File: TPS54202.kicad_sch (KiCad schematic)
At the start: 13 parts, among them U3 TPS54202DDC

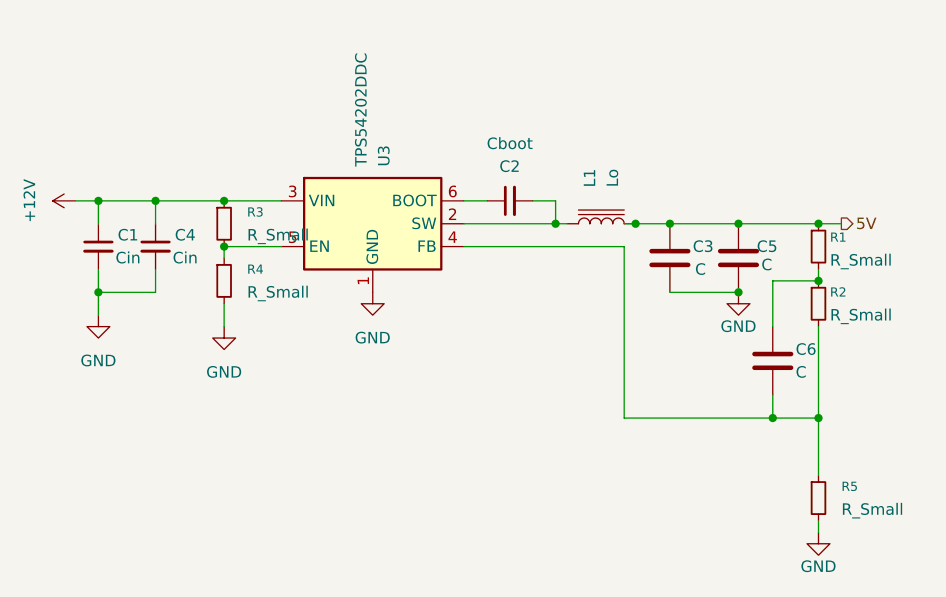
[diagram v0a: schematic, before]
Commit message: incomplete calcs for TPS
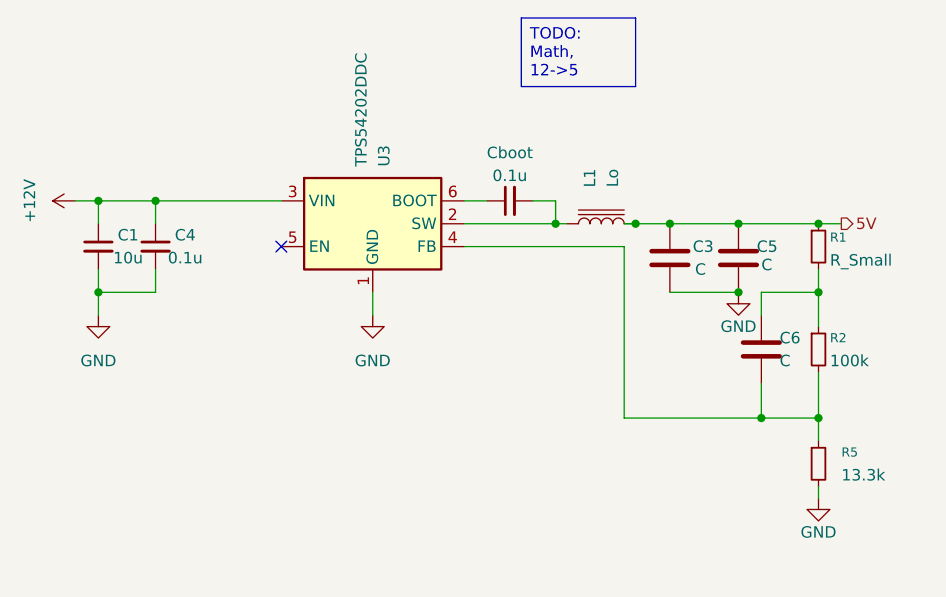
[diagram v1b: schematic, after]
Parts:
- removed R3, R4: R_Small, symbol Device:R_Small
- C1: value Cin -> 10u
- C4: value Cin -> 0.1u
- R2: value R_Small -> 100k
- R5: value R_Small -> 13.3k
- renumbered C2 to 0.1u
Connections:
- no-connect marks 0 -> 1
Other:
- moved on the sheet: C6, R2, R5

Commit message: finished math
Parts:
- removed R1: R_Small, symbol Device:R_Small
- C3, C5: value C -> 22u
- C6: value C -> 75p
- L1: value Lo -> 20u
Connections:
- net 5V: now also C6.1, R2.1
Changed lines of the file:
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@@
 	(generator_version "9.0")
 	(paper "A4")
-	(text_box "TODO: Math, 12->5\n"
+	(text_box "12->5 Iout = 1.5A"
 		(exclude_from_sim no)
 		(at 129.54 45.72 0)
-		(size 12.7 7.62)
+		(size 12.7 8.89)
 		(margins 0.9525 0.9525 0.9525 0.9525)
 		(stroke
@@
 	)
 	(junction
+		(at 162.56 68.58)
+		(diameter 0)
+		(color 0 0 0 0)
+	)
+	(junction
 		(at 82.55 66.04)
 		(diameter 0)
@@
 	)
 	(junction
-		(at 162.56 68.58)
-		(diameter 0)
-		(color 0 0 0 0)
-	)
-	(junction
 		(at 82.55 76.2)
 		(diameter 0)
@@
 	(wire
 		(pts
+			(xy 153.67 68.58) (xy 162.56 68.58)
+		)
+		(stroke
+			(width 0)
+			(type default)
+		)
+	)
+	(wire
+		(pts
+			(xy 162.56 92.71) (xy 162.56 90.17)
+		)
+		(stroke
+			(width 0)
+			(type default)
+		)
+	)
+	(wire
+		(pts
+			(xy 82.55 76.2) (xy 88.9 76.2)
+		)
+		(stroke
+			(width 0)
+			(type default)
+		)
+	)
+	(wire
+		(pts
 			(xy 162.56 68.58) (xy 165.1 68.58)
 		)
@@
 	(wire
 		(pts
-			(xy 162.56 92.71) (xy 162.56 90.17)
-		)
-		(stroke
-			(width 0)
-			(type default)
-		)
-	)
-	(wire
-		(pts
-			(xy 82.55 76.2) (xy 88.9 76.2)
-		)
-		(stroke
-			(width 0)
-			(type default)
-		)
-	)
-	(wire
-		(pts
 			(xy 142.24 68.58) (xy 146.05 68.58)
 		)
@@
 	(wire
 		(pts
-			(xy 153.67 68.58) (xy 162.56 68.58)
-		)
-		(stroke
-			(width 0)
-			(type default)
-		)
-	)
-	(wire
-		(pts
 			(xy 140.97 68.58) (xy 142.24 68.58)
 		)
@@
 	(wire
 		(pts
-			(xy 162.56 73.66) (xy 162.56 76.2)
+			(xy 162.56 68.58) (xy 162.56 76.2)
 		)
 		(stroke
@@
 			)
 		)
-		(property "Value" "C"
+		(property "Value" "22u"
 			(at 156.21 73.152 0)
 			(effects
@@
 			)
 		)
-		(property "Value" "Lo"
+		(property "Value" "20u"
 			(at 139.7 63.5 0)
 			(effects
@@
 	)
 	(symbol
-		(lib_id "Device:R_Small")
-		(at 162.56 71.12 0)
-		(unit 1)
-		(exclude_from_sim no)
-		(in_bom yes)
-		(on_board yes)
-		(dnp no)
-		(property "Reference" "R1"
-			(at 163.83 70.104 0)
-			(effects
-				(font
-					(size 1.016 1.016)
-				)
-				(justify left)
-			)
-		)
-		(property "Value" "R_Small"
-			(at 163.83 72.644 0)
-			(effects
-				(font
-					(size 1.27 1.27)
-				)
-				(justify left)
-			)
-		)
-		(property "Footprint" ""
-			(at 162.56 71.12 0)
-			(effects
-				(font
-					(size 1.27 1.27)
-				)
-				(hide yes)
-			)
-		)
-		(property "Datasheet" "~"
-			(at 162.56 71.12 0)
-			(effects
-				(font
-					(size 1.27 1.27)
-				)
-				(hide yes)
-			)
-		)
-		(property "Description" "Resistor, small symbol"
-			(at 162.56 71.12 0)
-			(effects
-				(font
-					(size 1.27 1.27)
-				)
-				(hide yes)
-			)
-		)
-		(pin "2"
-		)
-		(pin "1"
-		)
-		(instances
-			(project "LightsAndSuch"
-				(path "/f2987657-b7e0-480f-b307-23af9e47acd8/94c2b8e7-7d05-4ea8-a2a7-7484a2eccb30"
-					(reference "R1")
-					(unit 1)
-				)
-			)
-		)
-	)
-	(symbol
 		(lib_id "Device:C")
 		(at 156.21 82.55 0)
@@
 			)
 		)
-		(property "Value" "C"
+		(property "Value" "75p"
 			(at 158.242 83.82 0)
 			(effects
@@
 		(dnp no)
 		(property "Reference" "C3"
-			(at 148.59 71.12 0)
+			(at 147.828 71.12 0)
 			(effects
 				(font
@@
 			)
 		)
-		(property "Value" "C"
-			(at 148.844 73.6599 0)
-			(effects
-				(font
+		(property "Value" "22u"
+			(at 148.082 73.6599 0)
+			(effects
+				(font

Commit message: added secondary circuit
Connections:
- net 5V renamed +5V
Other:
- moved on the sheet: C1, C4
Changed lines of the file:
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@@
-	)
-	(junction
-		(at 82.55 66.04)
-		(diameter 0)
-		(color 0 0 0 0)
 	)
 	(junction
@@
 	)
 	(junction
+		(at 95.25 66.04)
+		(diameter 0)
+		(color 0 0 0 0)
+	)
+	(junction
 		(at 156.21 90.17)
 		(diameter 0)
@@
 	)
 	(junction
-		(at 82.55 76.2)
+		(at 88.9 76.2)
 		(diameter 0)
 		(color 0 0 0 0)
@@
 	(wire
 		(pts
-			(xy 82.55 66.04) (xy 88.9 66.04)
+			(xy 88.9 66.04) (xy 95.25 66.04)
 		)
 		(stroke
@@
 	(wire
 		(pts
-			(xy 82.55 76.2) (xy 82.55 78.74)
+			(xy 88.9 76.2) (xy 88.9 78.74)
 		)
 		(stroke
@@
 	(wire
 		(pts
-			(xy 82.55 66.04) (xy 80.01 66.04)
+			(xy 88.9 66.04) (xy 86.36 66.04)
 		)
 		(stroke
@@
 	(wire
 		(pts
-			(xy 82.55 73.66) (xy 82.55 76.2)
-		)
-		(stroke
-			(width 0)
-			(type default)
-		)
-	)
-	(wire
-		(pts
-			(xy 88.9 66.04) (xy 102.87 66.04)
+			(xy 88.9 73.66) (xy 88.9 76.2)
+		)
+		(stroke
+			(width 0)
+			(type default)
+		)
+	)
+	(wire
+		(pts
+			(xy 95.25 66.04) (xy 102.87 66.04)
 		)
 		(stroke
@@
 	(wire
 		(pts
+			(xy 95.25 66.04) (xy 95.25 68.58)
+		)
+		(stroke
+			(width 0)
+			(type default)
+		)
+	)
+	(wire
+		(pts
+			(xy 123.19 71.12) (xy 140.97 71.12)
+		)
+		(stroke
+			(width 0)
+			(type default)
+		)
+	)
+	(wire
+		(pts
+			(xy 162.56 85.09) (xy 162.56 90.17)
+		)
+		(stroke
+			(width 0)
+			(type default)
+		)
+	)
+	(wire
+		(pts
+			(xy 156.21 76.2) (xy 162.56 76.2)
+		)
+		(stroke
+			(width 0)
+			(type default)
+		)
+	)
+	(wire
+		(pts
 			(xy 88.9 66.04) (xy 88.9 68.58)
 		)
@@
 	(wire
 		(pts
-			(xy 123.19 71.12) (xy 140.97 71.12)
-		)
-		(stroke
-			(width 0)
-			(type default)
-		)
-	)
-	(wire
-		(pts
-			(xy 162.56 85.09) (xy 162.56 90.17)
-		)
-		(stroke
-			(width 0)
-			(type default)
-		)
-	)
-	(wire
-		(pts
-			(xy 156.21 76.2) (xy 162.56 76.2)
-		)
-		(stroke
-			(width 0)
-			(type default)
-		)
-	)
-	(wire
-		(pts
-			(xy 82.55 66.04) (xy 82.55 68.58)
-		)
-		(stroke
-			(width 0)
-			(type default)
-		)
-	)
-	(wire
-		(pts
 			(xy 146.05 68.58) (xy 153.67 68.58)
 		)
@@
 	(wire
 		(pts
-			(xy 82.55 76.2) (xy 88.9 76.2)
+			(xy 88.9 76.2) (xy 95.25 76.2)
 		)
 		(stroke
@@
 	(wire
 		(pts
-			(xy 88.9 73.66) (xy 88.9 76.2)
+			(xy 95.25 73.66) (xy 95.25 76.2)
 		)
 		(stroke
@@
 			(width 0)
 			(type default)
-		)
-	)
-	(hierarchical_label "5V"
-		(shape output)
-		(at 165.1 68.58 0)
-		(effects
-			(font
-				(size 1.27 1.27)
-			)
-			(justify left)
 		)
 	)
@@
 	(symbol
 		(lib_id "Device:C_Small")
-		(at 88.9 71.12 0)
+		(at 95.25 71.12 0)
 		(unit 1)
 		(exclude_from_sim no)
@@
 		(dnp no)
 		(property "Reference" "C4"
-			(at 92.202 69.85 0)
+			(at 98.552 69.85 0)
 			(effects
 				(font
@@
 		)
 		(property "Value" "0.1u"
-			(at 92.202 72.39 0)
+			(at 98.552 72.39 0)
 			(effects
 				(font
@@
 		)
 		(property "Footprint" ""
-			(at 88.9 71.12 0)
+			(at 95.25 71.12 0)
 			(effects
 				(font
@@
 		)
 		(property "Datasheet" "~"
-			(at 88.9 71.12 0)
+			(at 95.25 71.12 0)
 			(effects
 				(font
@@
 		)
 		(property "Description" "Unpolarized capacitor, small symbol"
-			(at 88.9 71.12 0)
+			(at 95.25 71.12 0)
 			(effects
 				(font
@@
 	(symbol
 		(lib_id "power:GND")
-		(at 82.55 78.74 0)
+		(at 88.9 78.74 0)
 		(unit 1)
 		(exclude_from_sim no)
@@
 		(fields_autoplaced yes)
 		(property "Reference" "#PWR05"
-			(at 82.55 85.09 0)
+			(at 88.9 85.09 0)
 			(effects
 				(font
@@
 		)
 		(property "Value" "GND"
-			(at 82.55 83.82 0)
+			(at 88.9 83.82 0)
 			(effects
 				(font
@@
 		)
 		(property "Footprint" ""
-			(at 82.55 78.74 0)
+			(at 88.9 78.74 0)
 			(effects
 				(font
@@
 		)
 		(property "Datasheet" ""
-			(at 82.55 78.74 0)
+			(at 88.9 78.74 0)
 			(effects
 				(font
@@
 		)
 		(property "Description" "Power symbol creates a global label with name \"GND\" , ground"
-			(at 82.55 78.74 0)
+			(at 88.9 78.74 0)
 			(effects
 				(font
@@
 	)
 	(symbol
+		(lib_id "power:+5V")
+		(at 165.1 68.58 270)
+		(unit 1)
+		(exclude_from_sim no)
+		(in_bom yes)
+		(on_board yes)
+		(dnp no)
+		(property "Reference" "#PWR022"
+			(at 161.29 68.58 0)
+			(effects
+				(font
+					(size 1.27 1.27)
+				)
+				(hide yes)
+			)
+		)
+		(property "Value" "+5V"
+			(at 170.18 68.58 0)
+			(effects
+				(font
+					(size 1.27 1.27)
+				)
+			)
+		)
+		(property "Footprint" ""
+			(at 165.1 68.58 0)
+			(effects
+				(font
+					(size 1.27 1.27)
+				)
+				(hide yes)
+			)
+		)
+		(property "Datasheet" ""
+			(at 165.1 68.58 0)
+			(effects
+				(font
+					(size 1.27 1.27)
+				)
+				(hide yes)
+			)
+		)
+		(property "Description" "Power symbol creates a global label with name \"+5V\""
+			(at 165.1 68.58 0)
+			(effects
+				(font
+					(size 1.27 1.27)
+				)
+				(hide yes)
+			)
+		)
+		(pin "1"
+		)
+		(instances
+			(project ""
+				(path "/f2987657-b7e0-480f-b307-23af9e47acd8/94c2b8e7-7d05-4ea8-a2a7-7484a2eccb30"
+					(reference "#PWR022")
+					(unit 1)
+				)
+			)
+		)
+	)
+	(symbol
 		(lib_id "power:+12V")
-		(at 80.01 66.04 90)
+		(at 86.36 66.04 90)
 		(unit 1)
 		(exclude_from_sim no)
@@
 		(fields_autoplaced yes)
 		(property "Reference" "#PWR01"
-			(at 83.82 66.04 0)
+			(at 90.17 66.04 0)
 			(effects
 				(font
@@
 		)
 		(property "Value" "+12V"
-			(at 74.93 66.04 0)
+			(at 81.28 66.04 0)
 			(effects
 				(font
@@
 		)
 		(property "Footprint" ""
-			(at 80.01 66.04 0)
+			(at 86.36 66.04 0)
 			(effects
 				(font
@@
 		)
 		(property "Datasheet" ""
-			(at 80.01 66.04 0)
+			(at 86.36 66.04 0)
 			(effects
 				(font
@@
 		)
 		(property "Description" "Power symbol creates a global label with name \"+12V\""
-			(at 80.01 66.04 0)
+			(at 86.36 66.04 0)
 			(effects
 				(font
@@
 	(symbol
 		(lib_id "Device:C_Small")
-		(at 82.55 71.12 0)
+		(at 88.9 71.12 0)
 		(unit 1)
 		(exclude_from_sim no)
@@
 		(dnp no)
 		(property "Reference" "C1"
-			(at 85.852 69.85 0)
+			(at 92.202 69.85 0)
 			(effects
 				(font
@@
 		)
 		(property "Value" "10u"
-			(at 85.852 72.39 0)
+			(at 92.202 72.39 0)
 			(effects
 				(font
@@
 		)
 		(property "Footprint" ""
-			(at 82.55 71.12 0)
+			(at 88.9 71.12 0)
 			(effects
 				(font
@@
 		)
 		(property "Datasheet" "~"
-			(at 82.55 71.12 0)
+			(at 88.9 71.12 0)
 			(effects
 				(font
@@
 		)
 		(property "Description" "Unpolarized capacitor, small symbol"
-			(at 82.55 71.12 0)
-			(effects
-				(font
+			(at 88.9 71.12 0)
+			(effects
+				(font
